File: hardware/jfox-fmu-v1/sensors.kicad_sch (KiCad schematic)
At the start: 5 parts, among them U1 ICM-42688-P, U2 ICM-45686, U3 BMI088, U4 BMP388, U5 FM25V02A

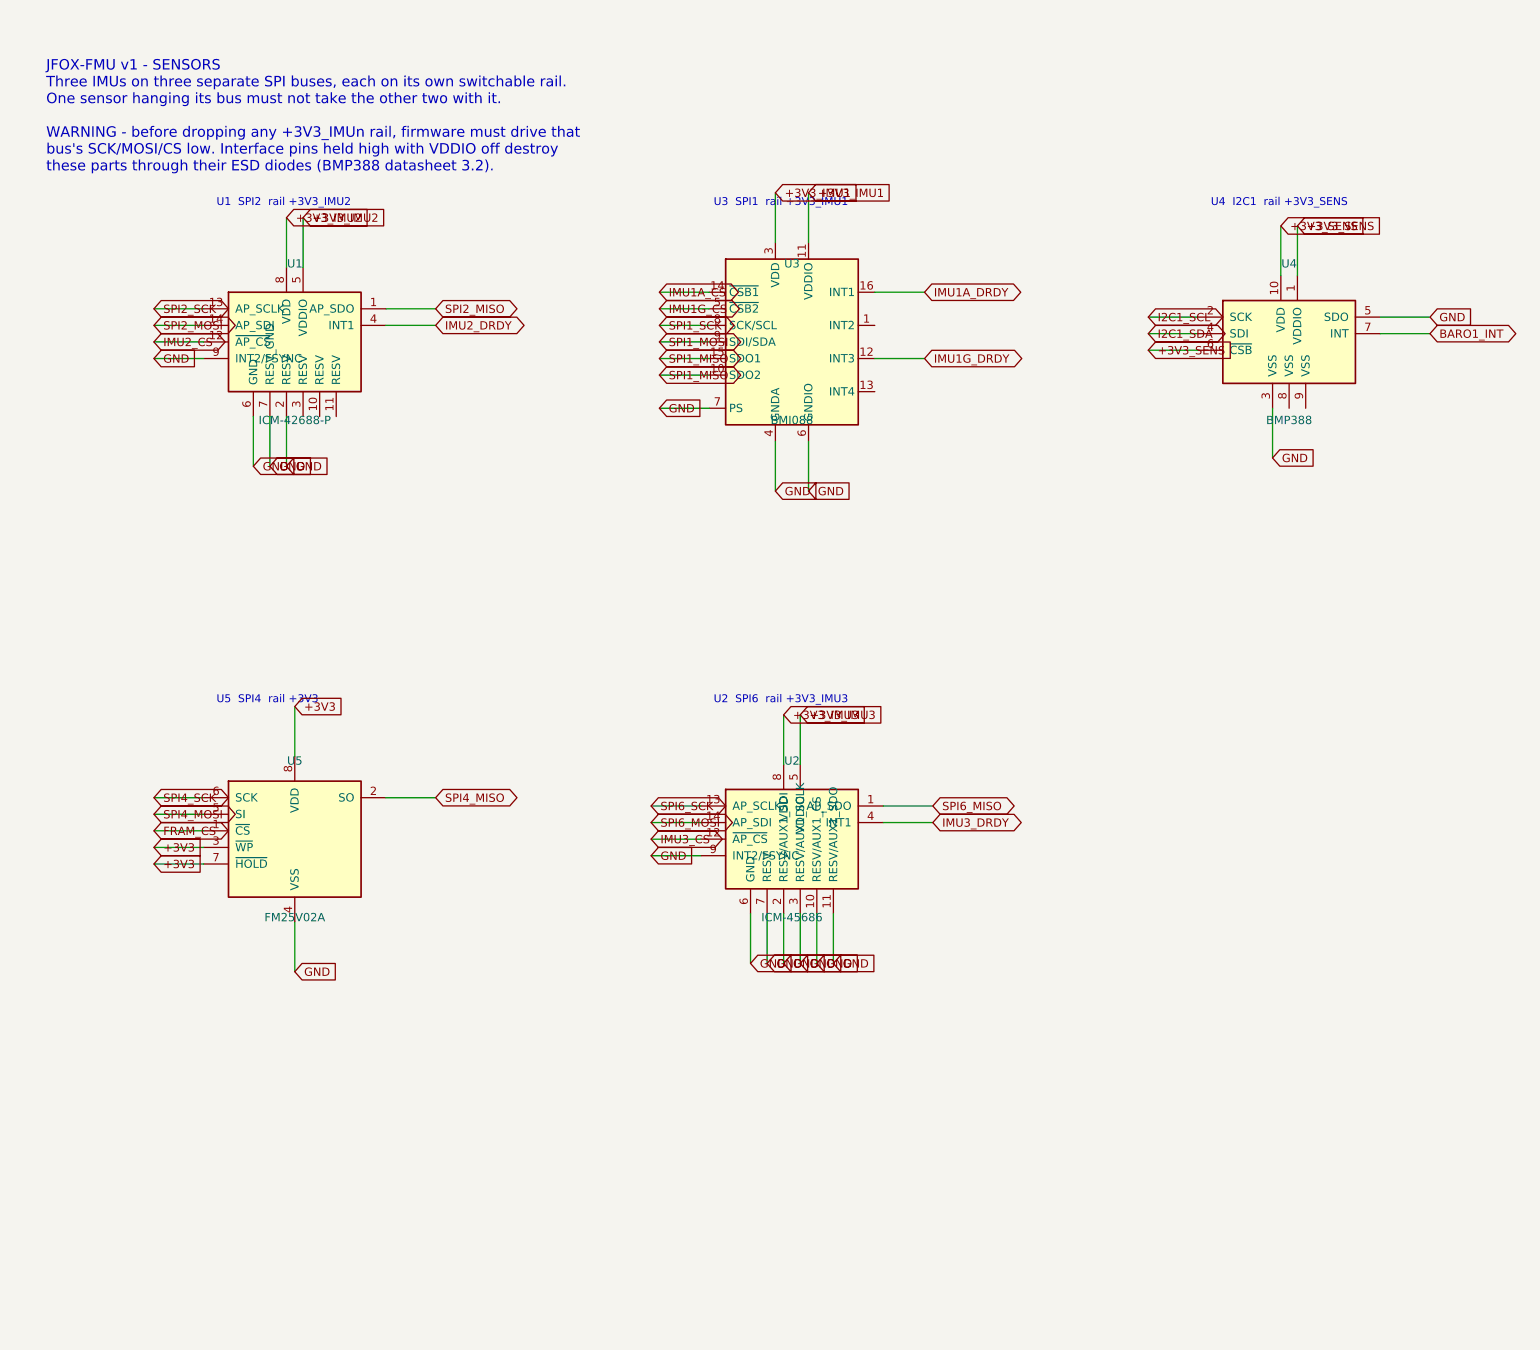
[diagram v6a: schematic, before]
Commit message: A4 title-blocked sheets, and the 25 power pins that were never wired
Every sheet now carries a title block naming JFOX Aircraft Co., Ltd., with a
per-sheet title, revision, date and the notes that used to float as loose text.

A4 PORTRAIT, not landscape, and not by preference. The STM32H753IITx symbol is
a single unit - KiCad's library gives it only _0_1 body and _1_1 pin
sub-symbols, so it cannot be split across pages - and its 176 pins span
231.1 mm. A4 landscape offers about 180 mm of usable height and would cut the
MCU in half. Portrait offers 237 mm. The part fits with 2 mm to spare, which
is why the page margin is 2 mm: it is the largest margin that still holds an
LQFP176, not a number chosen for looks.

The frame geometry was measured, not assumed - an empty A4 portrait sheet
plotted through kicad-cli, frame read off the SVG at 12,12 -> 198,285 with the
title block claiming x >= 90, y >= 253.

Three defects the work surfaced, in rising order of how much they mattered:

Every sheet had content at negative coordinates, off the page entirely, where
KiCad edits it happily and the plotter crops it away. Nothing had complained
because nothing was looking. fit() now translates each sheet into the drawable
area and refuses - loudly - to emit one that does not fit, because a schematic
that is silently cropped lies about the board.

fit() then passed the power sheet while its rightmost label sat 8.6 mm past
the frame. A global label's angle is the direction its CONNECTION faces, so
the text runs the opposite way; reading it the intuitive way put every
estimated extent on the wrong side of its anchor. That is worse than not
estimating: it reports "inside the frame" precisely when labels hang off it.
Caught by measuring KiCad's own plotted geometry instead of trusting the
estimate - which is what check_fmu_sheets.py now does on every sheet, with
--exclude-drawing-sheet so only the circuit is measured.

And centring the sheets by (SAFE_W - w) / 2 shifted every wire off th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
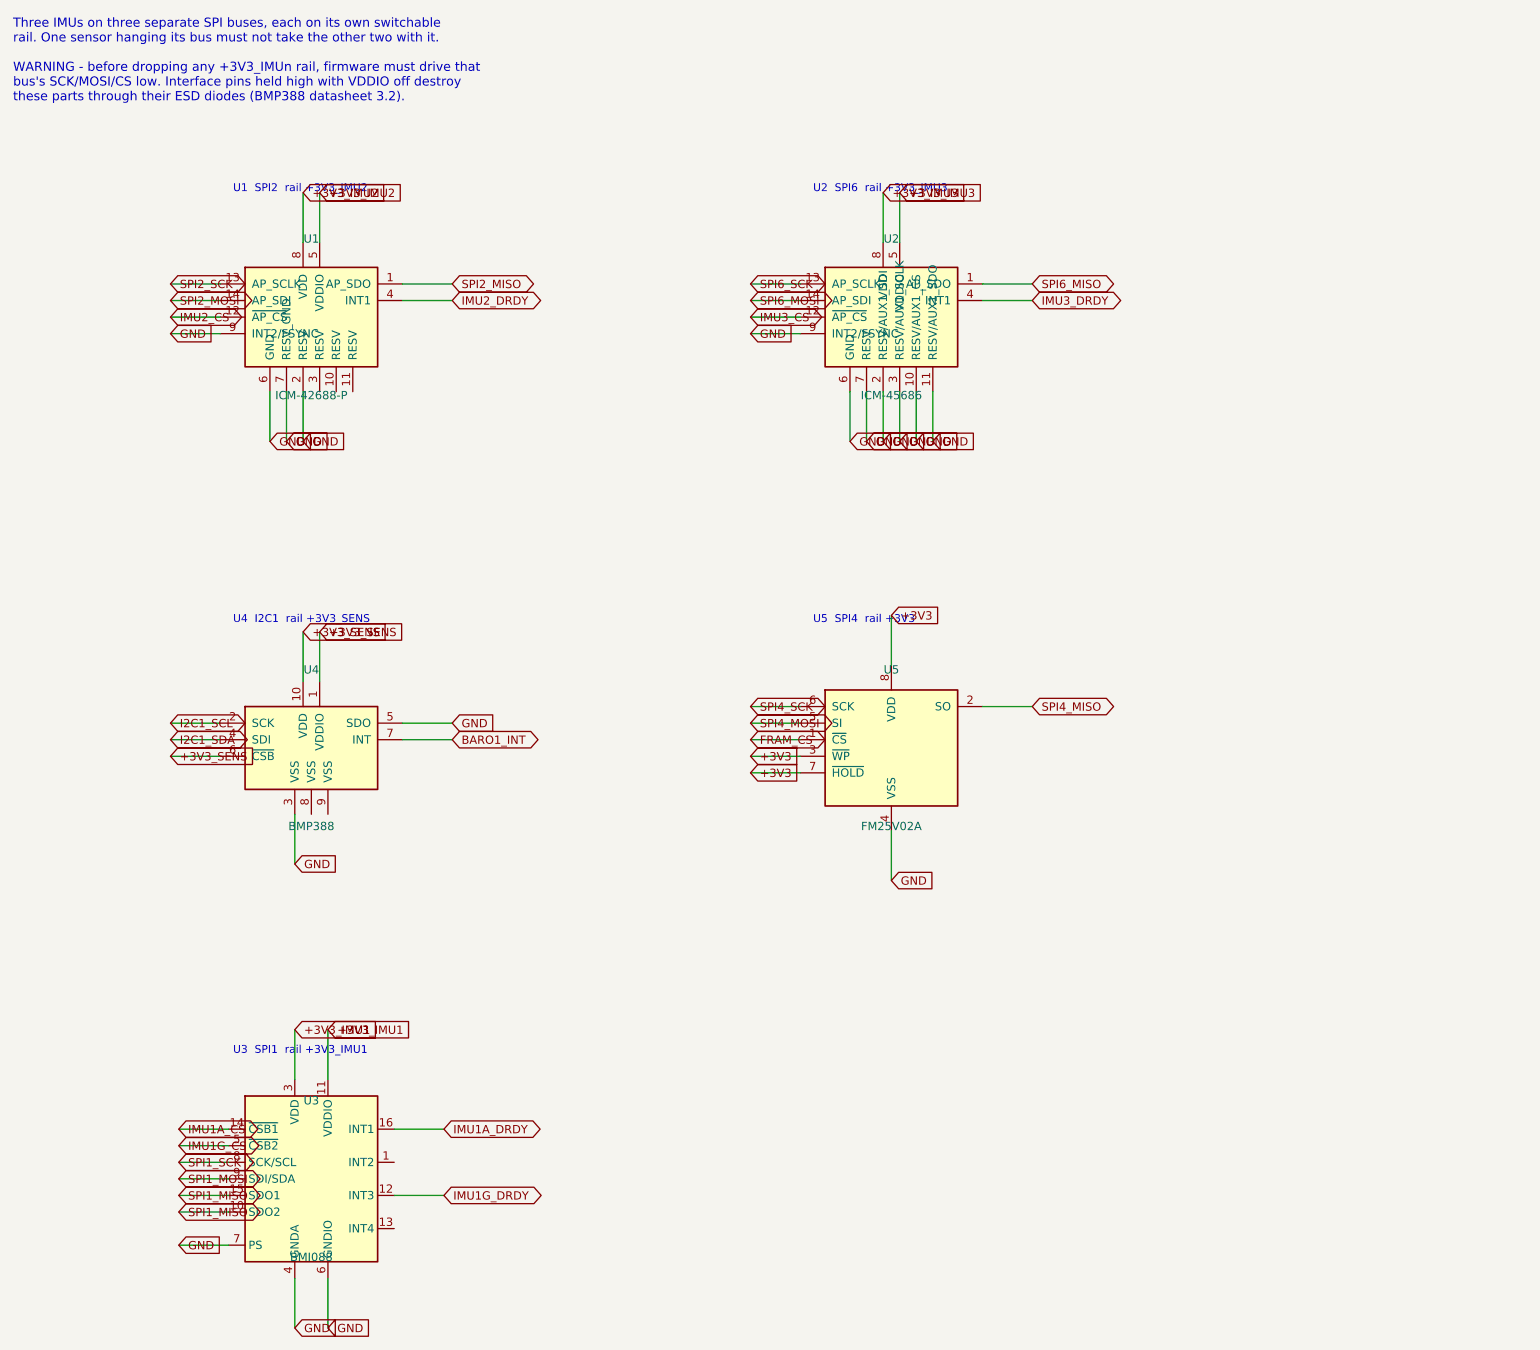
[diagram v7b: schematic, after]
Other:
- note added: "Three IMUs on three separate SPI buses, each on its own switchable rail. One sensor hanging its bus must not take the other two with it. WARNING - before dropping any +3V3_IMUn rail, firmware must drive that bus's SCK/MOSI/CS low. Interface pins held high with VDDIO off destroy these parts through their ESD diodes (BMP388 datasheet 3.2)."
- note removed: "JFOX-FMU v1 - SENSORS Three IMUs on three separate SPI buses, each on its own switchable rail. One sensor hanging its bus must not take the other two with it. WARNING - before dropping any +3V3_IMUn rail, firmware must drive that bus's SCK/MOSI/CS low. Interface pins held high with VDDIO off destroy these parts through their ESD diodes (BMP388 datasheet 3.2)."
- company: (none) -> JFOX Aircraft Co., Ltd.
- title: (none) -> Sensors
